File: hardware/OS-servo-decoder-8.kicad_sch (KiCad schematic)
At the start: 1 part, among them J101 FEMALE

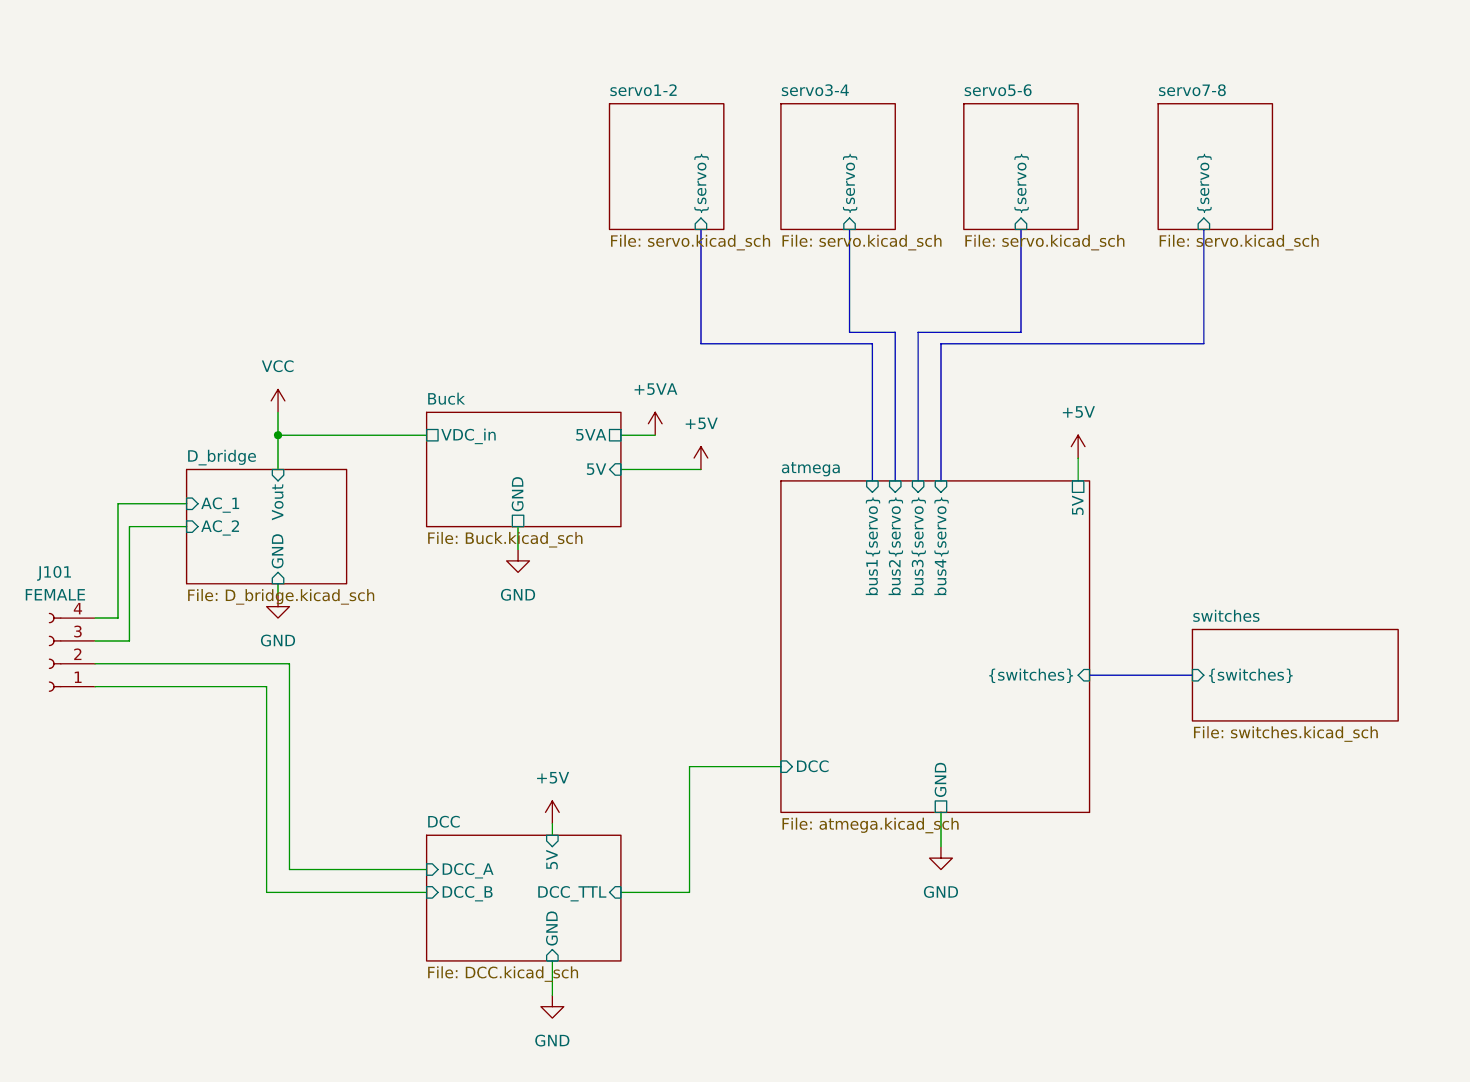
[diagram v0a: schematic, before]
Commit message: update board file, made similar to OS solenoid decoder
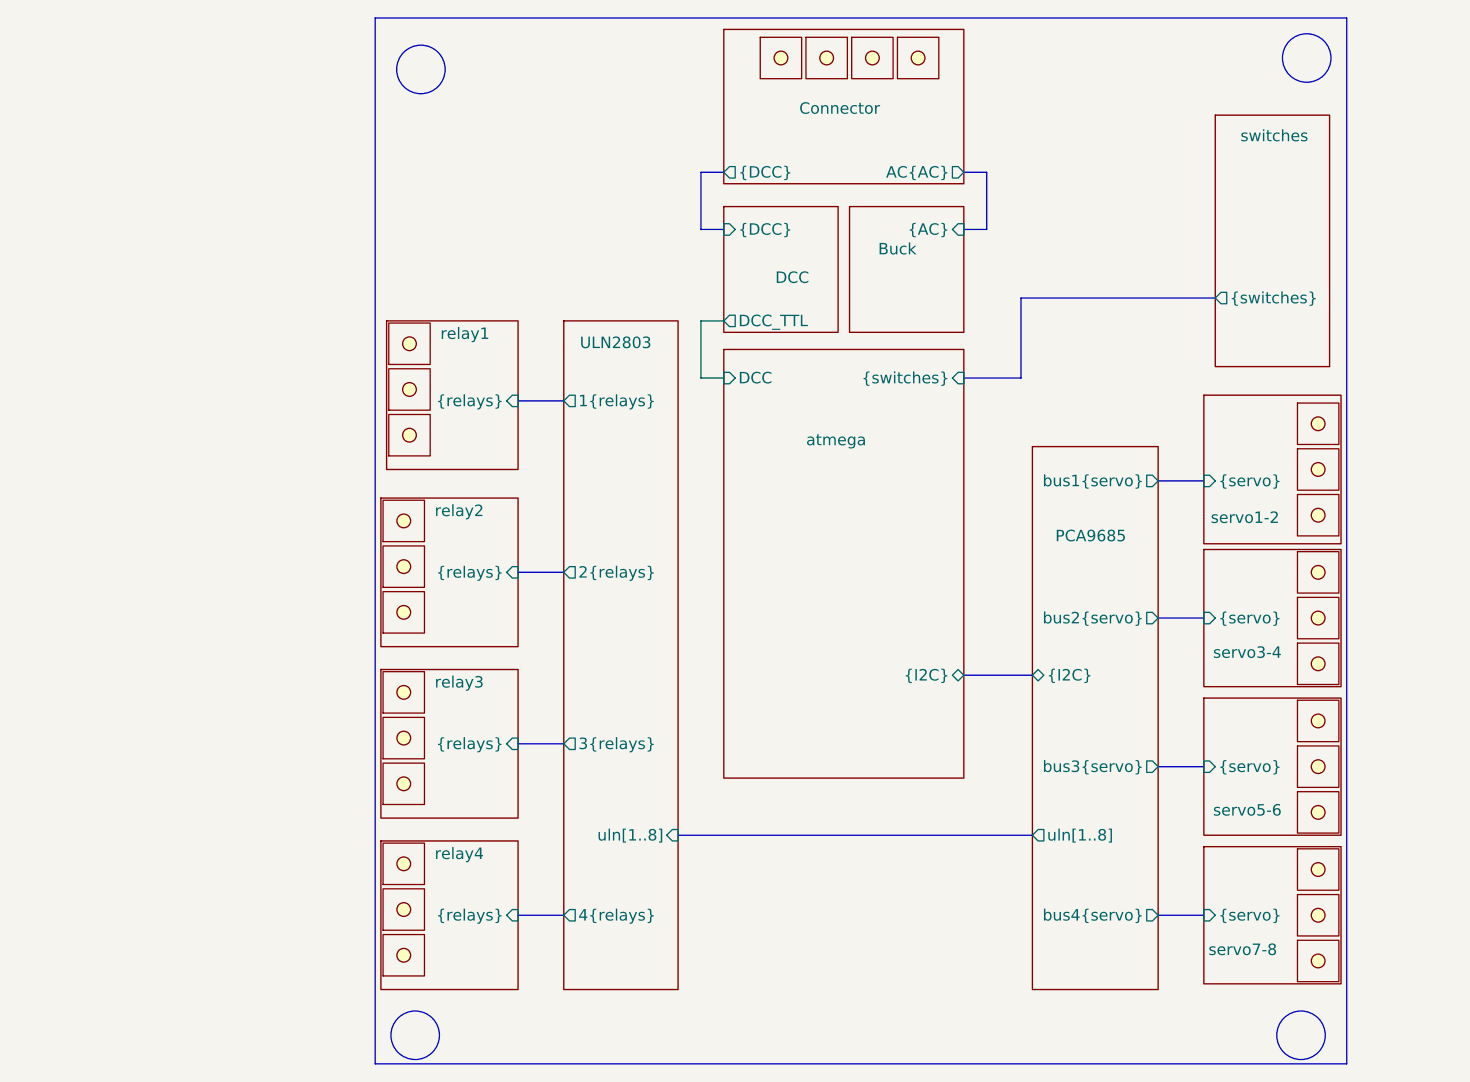
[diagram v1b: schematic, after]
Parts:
- removed J101: FEMALE, Connector_Phoenix_MC:PhoenixContact_MC_1,5_4-G-3.5_1x04_P3.50mm_Horizontal, symbol custom_kicad_lib_sk:connector_3.50mm_4P_horizontal_FEMALE
- added u101, u102, u103, u104, u105, u106, u107, u108, u109, u110, u111, u112, u113, u114, u115, u116, u117, u118, u119, u120, u121, u122, u123, u124, u125, u126, u127, u128: ~, symbol custom_kicad_lib_sk:screwterminal
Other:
- removed sheet D_bridge
- added sheet Connector (Connector.kicad_sch)
- added sheet PCA9685 (PCA9685.kicad_sch)
- added sheet ULN2803 (ULN2803.kicad_sch)
- added sheet relay1 (relayConnector.kicad_sch)
- added sheet relay2 (relayConnector.kicad_sch)
- added sheet relay3 (relayConnector.kicad_sch)
- added sheet relay4 (relayConnector.kicad_sch)
- sheet Buck ports: added {AC}; removed 5V, 5VA, GND, VDC_in
- sheet DCC ports: added {DCC}; removed 5V, DCC_A, DCC_B, GND
- sheet atmega ports: added {I2C}; removed 5V, GND, bus1{servo}, bus2{servo}, bus3{servo}, bus4{servo}
